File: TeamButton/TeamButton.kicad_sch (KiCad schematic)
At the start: 0 parts

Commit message: Bring in old schematic for cleanup / base work.
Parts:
- added J1: RJ45, symbol Connector:RJ45
- added SW1, SW2: SW_Push, symbol Switch:SW_Push
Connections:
- new net: J1.4, SW2.1
- new net: J1.3, SW2.2
- new net: J1.8, SW1.1
- new net: J1.7, SW1.2
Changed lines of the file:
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@@
 (kicad_sch (version 20221206) (generator eeschema)
   (paper "A4")
-  (symbol_instances)
+  (wire (pts (xy 104.14 72.39) (xy 123.19 72.39))
+    (stroke (width 0) (type default))
+  )
+  (wire (pts (xy 113.03 69.85) (xy 104.14 69.85))
+    (stroke (width 0) (type default))
+  )
+  (wire (pts (xy 123.19 82.55) (xy 104.14 82.55))
+    (stroke (width 0) (type default))
+  )
+  (wire (pts (xy 123.19 72.39) (xy 123.19 69.85))
+    (stroke (width 0) (type default))
+  )
+  (wire (pts (xy 104.14 80.01) (xy 113.03 80.01))
+    (stroke (width 0) (type default))
+  )
+  (wire (pts (xy 123.19 80.01) (xy 123.19 82.55))
+    (stroke (width 0) (type default))
+  )
+  (symbol (lib_id "Switch:SW_Push") (at 118.11 80.01 0) (unit 1)
+    (in_bom yes) (on_board yes) (dnp no) (fields_autoplaced)
+    (property "Reference" "SW2" (at 118.11 73.66 0)
+      (effects (font (size 1.27 1.27)))
+    )
+    (property "Value" "SW_Push" (at 118.11 76.2 0)
+      (effects (font (size 1.27 1.27)))
+    )
+    (property "Footprint" "" (at 118.11 74.93 0)
+      (effects (font (size 1.27 1.27)) hide)
+    )
+    (property "Datasheet" "~" (at 118.11 74.93 0)
+      (effects (font (size 1.27 1.27)) hide)
+    )
+    (pin "1")
+    (pin "2")
+    (instances
+      (project "TeamButton"
+        (path "/a2251e9b-34a9-4b44-9287-d557388f6936"
+          (reference "SW2") (unit 1)
+        )
+      )
+    )
+  )
+  (symbol (lib_id "Switch:SW_Push") (at 118.11 69.85 0) (unit 1)
+    (in_bom yes) (on_board yes) (dnp no) (fields_autoplaced)
+    (property "Reference" "SW1" (at 118.11 63.5 0)
+      (effects (font (size 1.27 1.27)))
+    )
+    (property "Value" "SW_Push" (at 118.11 66.04 0)
+      (effects (font (size 1.27 1.27)))
+    )
+    (property "Footprint" "" (at 118.11 64.77 0)
+      (effects (font (size 1.27 1.27)) hide)
+    )
+    (property "Datasheet" "~" (at 118.11 64.77 0)
+      (effects (font (size 1.27 1.27)) hide)
+    )
+    (pin "1")
+    (pin "2")
+    (instances
+      (project "TeamButton"
+        (path "/a2251e9b-34a9-4b44-9287-d557388f6936"
+          (reference "SW1") (unit 1)
+        )
+      )
+    )
+  )
+  (symbol (lib_id "Connector:RJ45") (at 93.98 80.01 0) (unit 1)
+    (in_bom yes) (on_board yes) (dnp no) (fields_autoplaced)
+    (property "Reference" "J1" (at 93.98 63.5 0)
+      (effects (font (size 1.27 1.27)))
+    )
+    (property "Value" "RJ45" (at 93.98 66.04 0)
+      (effects (font (size 1.27 1.27)))
+    )
+    (property "Footprint" "" (at 93.98 79.375 90)
+      (effects (font (size 1.27 1.27)) hide)
+    )
+    (property "Datasheet" "~" (at 93.98 79.375 90)
+      (effects (font (size 1.27 1.27)) hide)
+    )
+    (pin "1")
+    (pin "2")
+    (pin "3")
+    (pin "4")
+    (pin "5")
+    (pin "6")
+    (pin "7")
+    (pin "8")
+    (instances
+      (project "TeamButton"
+        (path "/a2251e9b-34a9-4b44-9287-d557388f6936"
+          (reference "J1") (unit 1)
+        )
+      )
+    )
+  )
+  (sheet_instances
+    (path "/" (page "1"))
+  )
 )

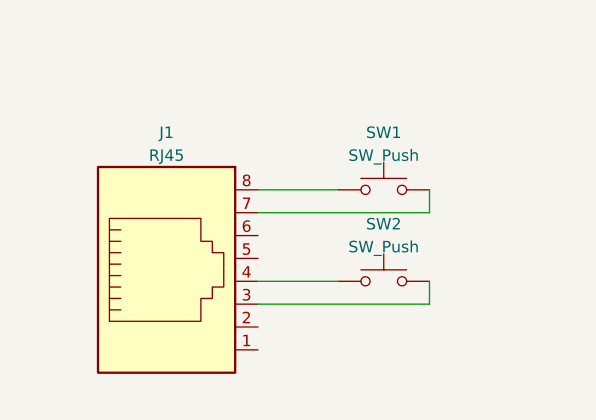
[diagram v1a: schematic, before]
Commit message: Added new files, swap to new FET for toggling, added FET as symbols.
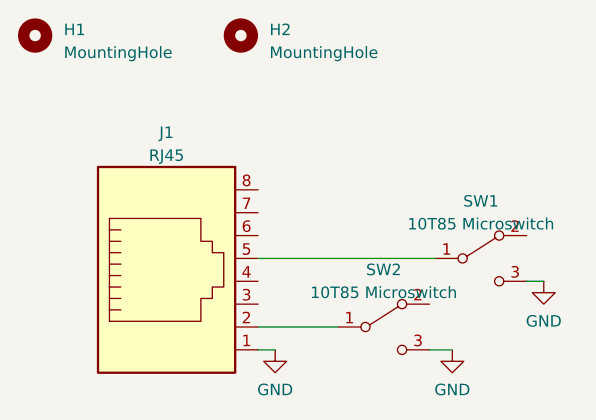
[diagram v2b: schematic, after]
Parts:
- removed SW1, SW2: SW_Push, symbol Switch:SW_Push
- added H1, H2: MountingHole, MountingHole:MountingHole_2.7mm_M2.5_DIN965, symbol Mechanical:MountingHole
- added SW1, SW2: 10T85 Microswitch, footprints:10T85 Microswitch, symbol symbols:10T85 Microswitch
- J1: footprint (none) -> footprints:RCH RC00139
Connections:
- net GND: now reaches J1.1
- net GND: now also SW1.3 (NO), SW2.3 (NO)
- net at J1.2: now also SW2.1 (C)
- net at J1.5: now also SW1.1 (C)
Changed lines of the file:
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@@
-(kicad_sch (version 20221206) (generator eeschema)
+(kicad_sch (version 20230121) (generator eeschema)
   (paper "A4")
-  (wire (pts (xy 104.14 72.39) (xy 123.19 72.39))
+  (wire (pts (xy 104.14 77.47) (xy 123.825 77.47))
     (stroke (width 0) (type default))
   )
-  (wire (pts (xy 113.03 69.85) (xy 104.14 69.85))
+  (wire (pts (xy 104.14 87.63) (xy 106.045 87.63))
     (stroke (width 0) (type default))
   )
-  (wire (pts (xy 123.19 82.55) (xy 104.14 82.55))
+  (wire (pts (xy 104.14 85.09) (xy 113.03 85.09))
     (stroke (width 0) (type default))
   )
-  (wire (pts (xy 123.19 72.39) (xy 123.19 69.85))
+  (wire (pts (xy 135.89 80.01) (xy 133.985 80.01))
     (stroke (width 0) (type default))
   )
-  (wire (pts (xy 104.14 80.01) (xy 113.03 80.01))
+  (wire (pts (xy 125.73 87.63) (xy 123.19 87.63))
     (stroke (width 0) (type default))
   )
-  (wire (pts (xy 123.19 80.01) (xy 123.19 82.55))
-    (stroke (width 0) (type default))
-  )
-  (symbol (lib_id "Switch:SW_Push") (at 118.11 80.01 0) (unit 1)
+  (symbol (lib_id "power:GND") (at 125.73 87.63 0) (unit 1)
     (in_bom yes) (on_board yes) (dnp no) (fields_autoplaced)
-    (property "Reference" "SW2" (at 118.11 73.66 0)
+    (property "Reference" "#PWR04" (at 125.73 93.98 0)
+      (effects (font (size 1.27 1.27)) hide)
+    )
+    (property "Value" "GND" (at 125.73 92.075 0)
       (effects (font (size 1.27 1.27)))
     )
-    (property "Value" "SW_Push" (at 118.11 76.2 0)
+    (property "Footprint" "" (at 125.73 87.63 0)
+      (effects (font (size 1.27 1.27)) hide)
+    )
+    (property "Datasheet" "" (at 125.73 87.63 0)
+      (effects (font (size 1.27 1.27)) hide)
+    )
+    (pin "1")
+    (instances
+      (project "TeamButton"
+        (path "/a2251e9b-34a9-4b44-9287-d557388f6936"
+          (reference "#PWR04") (unit 1)
+        )
+      )
+    )
+  )
+  (symbol (lib_id "power:GND") (at 106.045 87.63 0) (unit 1)
+    (in_bom yes) (on_board yes) (dnp no) (fields_autoplaced)
+    (property "Reference" "#PWR03" (at 106.045 93.98 0)
+      (effects (font (size 1.27 1.27)) hide)
+    )
+    (property "Value" "GND" (at 106.045 92.075 0)
       (effects (font (size 1.27 1.27)))
     )
-    (property "Footprint" "" (at 118.11 74.93 0)
+    (property "Footprint" "" (at 106.045 87.63 0)
       (effects (font (size 1.27 1.27)) hide)
     )
-    (property "Datasheet" "~" (at 118.11 74.93 0)
+    (property "Datasheet" "" (at 106.045 87.63 0)
+      (effects (font (size 1.27 1.27)) hide)
+    )
+    (pin "1")
+    (instances
+      (project "TeamButton"
+        (path "/a2251e9b-34a9-4b44-9287-d557388f6936"
+          (reference "#PWR03") (unit 1)
+        )
+      )
+    )
+  )
+  (symbol (lib_id "Mechanical:MountingHole") (at 79.375 52.705 0) (unit 1)
+    (in_bom yes) (on_board yes) (dnp no) (fields_autoplaced)
+    (property "Reference" "H1" (at 82.55 52.07 0)
+      (effects (font (size 1.27 1.27)) (justify left))
+    )
+    (property "Value" "MountingHole" (at 82.55 54.61 0)
+      (effects (font (size 1.27 1.27)) (justify left))
+    )
+    (property "Footprint" "MountingHole:MountingHole_2.7mm_M2.5_DIN965" (at 79.375 52.705 0)
+      (effects (font (size 1.27 1.27)) hide)
+    )
+    (property "Datasheet" "~" (at 79.375 52.705 0)
+      (effects (font (size 1.27 1.27)) hide)
+    )
+    (instances
+      (project "TeamButton"
+        (path "/a2251e9b-34a9-4b44-9287-d557388f6936"
+          (reference "H1") (unit 1)
+        )
+      )
+    )
+  )
+  (symbol (lib_id "symbols:10T85 Microswitch") (at 118.11 85.09 0) (unit 1)
+    (in_bom yes) (on_board yes) (dnp no) (fields_autoplaced)
+    (property "Reference" "SW2" (at 118.11 78.74 0)
+      (effects (font (size 1.27 1.27)))
+    )
+    (property "Value" "10T85 Microswitch" (at 118.11 81.28 0)
+      (effects (font (size 1.27 1.27)))
+    )
+    (property "Footprint" "footprints:10T85 Microswitch" (at 118.11 92.71 0)
+      (effects (font (size 1.27 1.27)) hide)
+    )
+    (property "Datasheet" "~" (at 118.11 85.09 0)
       (effects (font (size 1.27 1.27)) hide)
     )
     (pin "1")
     (pin "2")
+    (pin "3")
     (instances
       (project "TeamButton"
@@
     )
   )
-  (symbol (lib_id "Switch:SW_Push") (at 118.11 69.85 0) (unit 1)
+  (symbol (lib_id "power:GND") (at 135.89 80.01 0) (unit 1)
     (in_bom yes) (on_board yes) (dnp no) (fields_autoplaced)
-    (property "Reference" "SW1" (at 118.11 63.5 0)
+    (property "Reference" "#PWR05" (at 135.89 86.36 0)
+      (effects (font (size 1.27 1.27)) hide)
+    )
+    (property "Value" "GND" (at 135.89 84.455 0)
       (effects (font (size 1.27 1.27)))
     )
-    (property "Value" "SW_Push" (at 118.11 66.04 0)
+    (property "Footprint" "" (at 135.89 80.01 0)
+      (effects (font (size 1.27 1.27)) hide)
+    )
+    (property "Datasheet" "" (at 135.89 80.01 0)
+      (effects (font (size 1.27 1.27)) hide)
+    )
+    (pin "1")
+    (instances
+      (project "TeamButton"
+        (path "/a2251e9b-34a9-4b44-9287-d557388f6936"
+          (reference "#PWR05") (unit 1)
+        )
+      )
+    )
+  )
+  (symbol (lib_id "Mechanical:MountingHole") (at 102.235 52.705 0) (unit 1)
+    (in_bom yes) (on_board yes) (dnp no) (fields_autoplaced)
+    (property "Reference" "H2" (at 105.41 52.07 0)
+      (effects (font (size 1.27 1.27)) (justify left))
+    )
+    (property "Value" "MountingHole" (at 105.41 54.61 0)
+      (effects (font (size 1.27 1.27)) (justify left))
+    )
+    (property "Footprint" "MountingHole:MountingHole_2.7mm_M2.5_DIN965" (at 102.235 52.705 0)
+      (effects (font (size 1.27 1.27)) hide)
+    )
+    (property "Datasheet" "~" (at 102.235 52.705 0)
+      (effects (font (size 1.27 1.27)) hide)
+    )
+    (instances
+      (project "TeamButton"
+        (path "/a2251e9b-34a9-4b44-9287-d557388f6936"
+          (reference "H2") (unit 1)
+        )
+      )
+    )
+  )
+  (symbol (lib_id "symbols:10T85 Microswitch") (at 128.905 77.47 0) (unit 1)
+    (in_bom yes) (on_board yes) (dnp no) (fields_autoplaced)
+    (property "Reference" "SW1" (at 128.905 71.12 0)
       (effects (font (size 1.27 1.27)))
     )
-    (property "Footprint" "" (at 118.11 64.77 0)
+    (property "Value" "10T85 Microswitch" (at 128.905 73.66 0)
+      (effects (font (size 1.27 1.27)))
+    )
+    (property "Footprint" "footprints:10T85 Microswitch" (at 128.905 85.09 0)
       (effects (font (size 1.27 1.27)) hide)
     )
-    (property "Datasheet" "~" (at 118.11 64.77 0)
+    (property "Datasheet" "~" (at 128.905 77.47 0)
       (effects (font (size 1.27 1.27)) hide)
     )
     (pin "1")
     (pin "2")
+    (pin "3")
     (instances
       (project "TeamButton"
@@
       (effects (font (size 1.27 1.27)))
     )
-    (property "Footprint" "" (at 93.98 79.375 90)
+    (property "Footprint" "footprints:RCH RC00139" (at 93.98 79.375 90)
       (effects (font (size 1.27 1.27)) hide)
     )

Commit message: Updated team buttonboard to use M3 fasteners!
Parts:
- H1, H2: footprint MountingHole:MountingHole_2.7mm_M2.5_DIN965 -> MountingHole:MountingHole_3.2mm_M3
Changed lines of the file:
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@@
       (effects (font (size 1.27 1.27)) (justify left))
     )
-    (property "Footprint" "MountingHole:MountingHole_2.7mm_M2.5_DIN965" (at 79.375 52.705 0)
+    (property "Footprint" "MountingHole:MountingHole_3.2mm_M3" (at 79.375 52.705 0)
       (effects (font (size 1.27 1.27)) hide)
     )
@@
       (effects (font (size 1.27 1.27)) (justify left))
     )
-    (property "Footprint" "MountingHole:MountingHole_2.7mm_M2.5_DIN965" (at 102.235 52.705 0)
+    (property "Footprint" "MountingHole:MountingHole_3.2mm_M3" (at 102.235 52.705 0)
       (effects (font (size 1.27 1.27)) hide)
     )

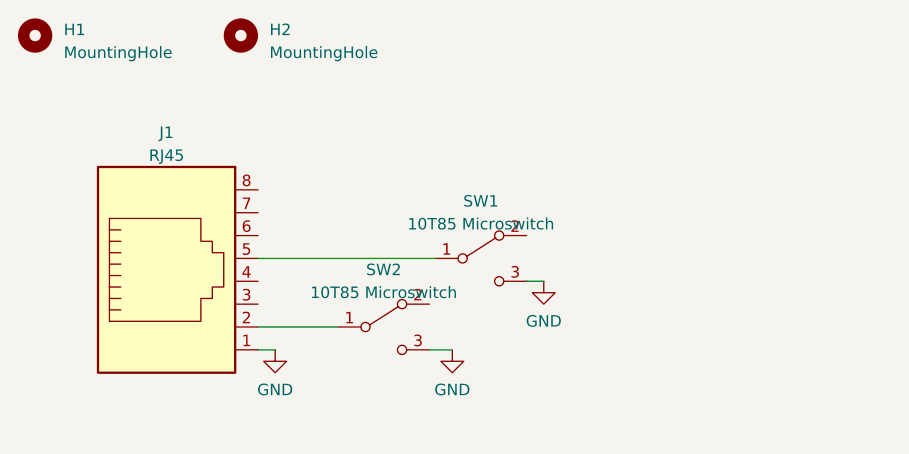
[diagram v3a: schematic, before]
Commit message: Updated Button and Stacklight PCB to not have backwards fucking footprint shit.
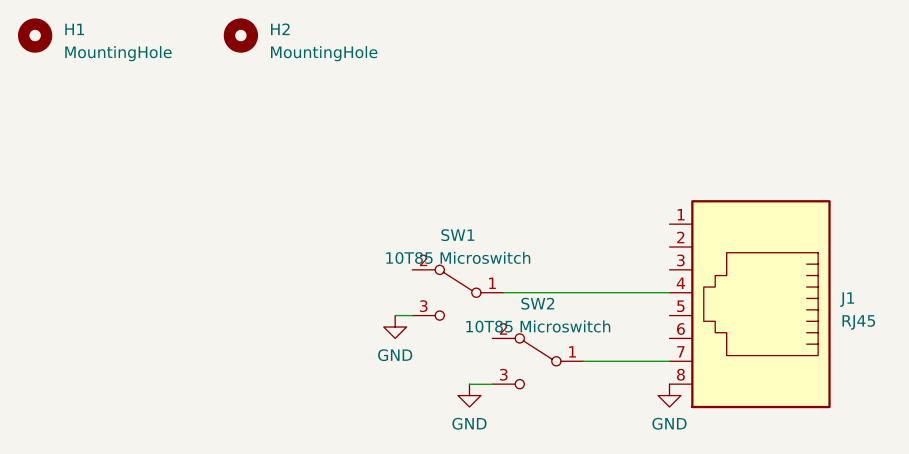
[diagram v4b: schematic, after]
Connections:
- net GND: now also J1.8; no longer J1.1
- net at SW2.1 (C): now also J1.7; no longer J1.2
- net at SW1.1 (C): now also J1.4; no longer J1.5
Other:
- moved on the sheet: J1, SW1, SW2
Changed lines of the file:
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@@
 (kicad_sch (version 20230121) (generator eeschema)
   (paper "A4")
-  (wire (pts (xy 104.14 77.47) (xy 123.825 77.47))
+  (wire (pts (xy 140.335 88.9) (xy 149.86 88.9))
     (stroke (width 0) (type default))
   )
-  (wire (pts (xy 104.14 87.63) (xy 106.045 87.63))
+  (wire (pts (xy 119.38 83.82) (xy 121.285 83.82))
     (stroke (width 0) (type default))
   )
-  (wire (pts (xy 104.14 85.09) (xy 113.03 85.09))
+  (wire (pts (xy 127.635 91.44) (xy 130.175 91.44))
     (stroke (width 0) (type default))
   )
-  (wire (pts (xy 135.89 80.01) (xy 133.985 80.01))
+  (wire (pts (xy 131.445 81.28) (xy 149.86 81.28))
     (stroke (width 0) (type default))
   )
-  (wire (pts (xy 125.73 87.63) (xy 123.19 87.63))
-    (stroke (width 0) (type default))
-  )
-  (symbol (lib_id "power:GND") (at 125.73 87.63 0) (unit 1)
+  (symbol (lib_id "power:GND") (at 127.635 91.44 0) (mirror y) (unit 1)
     (in_bom yes) (on_board yes) (dnp no) (fields_autoplaced)
-    (property "Reference" "#PWR04" (at 125.73 93.98 0)
+    (property "Reference" "#PWR04" (at 127.635 97.79 0)
       (effects (font (size 1.27 1.27)) hide)
     )
-    (property "Value" "GND" (at 125.73 92.075 0)
+    (property "Value" "GND" (at 127.635 95.885 0)
       (effects (font (size 1.27 1.27)))
     )
-    (property "Footprint" "" (at 125.73 87.63 0)
+    (property "Footprint" "" (at 127.635 91.44 0)
       (effects (font (size 1.27 1.27)) hide)
     )
-    (property "Datasheet" "" (at 125.73 87.63 0)
+    (property "Datasheet" "" (at 127.635 91.44 0)
       (effects (font (size 1.27 1.27)) hide)
     )
@@
     )
   )
-  (symbol (lib_id "power:GND") (at 106.045 87.63 0) (unit 1)
+  (symbol (lib_id "power:GND") (at 149.86 91.44 0) (unit 1)
     (in_bom yes) (on_board yes) (dnp no) (fields_autoplaced)
-    (property "Reference" "#PWR03" (at 106.045 93.98 0)
+    (property "Reference" "#PWR03" (at 149.86 97.79 0)
       (effects (font (size 1.27 1.27)) hide)
     )
-    (property "Value" "GND" (at 106.045 92.075 0)
+    (property "Value" "GND" (at 149.86 95.885 0)
       (effects (font (size 1.27 1.27)))
     )
-    (property "Footprint" "" (at 106.045 87.63 0)
+    (property "Footprint" "" (at 149.86 91.44 0)
       (effects (font (size 1.27 1.27)) hide)
     )
-    (property "Datasheet" "" (at 106.045 87.63 0)
+    (property "Datasheet" "" (at 149.86 91.44 0)
       (effects (font (size 1.27 1.27)) hide)
     )
@@
     )
   )
-  (symbol (lib_id "symbols:10T85 Microswitch") (at 118.11 85.09 0) (unit 1)
+  (symbol (lib_id "symbols:10T85 Microswitch") (at 135.255 88.9 0) (mirror y) (unit 1)
     (in_bom yes) (on_board yes) (dnp no) (fields_autoplaced)
-    (property "Reference" "SW2" (at 118.11 78.74 0)
+    (property "Reference" "SW2" (at 135.255 82.55 0)
       (effects (font (size 1.27 1.27)))
     )
-    (property "Value" "10T85 Microswitch" (at 118.11 81.28 0)
+    (property "Value" "10T85 Microswitch" (at 135.255 85.09 0)
       (effects (font (size 1.27 1.27)))
     )
-    (property "Footprint" "footprints:10T85 Microswitch" (at 118.11 92.71 0)
+    (property "Footprint" "footprints:10T85 Microswitch" (at 135.255 96.52 0)
       (effects (font (size 1.27 1.27)) hide)
     )
-    (property "Datasheet" "~" (at 118.11 85.09 0)
+    (property "Datasheet" "~" (at 135.255 88.9 0)
       (effects (font (size 1.27 1.27)) hide)
     )
@@
     )
   )
-  (symbol (lib_id "power:GND") (at 135.89 80.01 0) (unit 1)
+  (symbol (lib_id "power:GND") (at 119.38 83.82 0) (mirror y) (unit 1)
     (in_bom yes) (on_board yes) (dnp no) (fields_autoplaced)
-    (property "Reference" "#PWR05" (at 135.89 86.36 0)
+    (property "Reference" "#PWR05" (at 119.38 90.17 0)
       (effects (font (size 1.27 1.27)) hide)
     )
-    (property "Value" "GND" (at 135.89 84.455 0)
+    (property "Value" "GND" (at 119.38 88.265 0)
       (effects (font (size 1.27 1.27)))
     )
-    (property "Footprint" "" (at 135.89 80.01 0)
+    (property "Footprint" "" (at 119.38 83.82 0)
       (effects (font (size 1.27 1.27)) hide)
     )
-    (property "Datasheet" "" (at 135.89 80.01 0)
+    (property "Datasheet" "" (at 119.38 83.82 0)
       (effects (font (size 1.27 1.27)) hide)
     )
@@
     )
   )
-  (symbol (lib_id "symbols:10T85 Microswitch") (at 128.905 77.47 0) (unit 1)
+  (symbol (lib_id "symbols:10T85 Microswitch") (at 126.365 81.28 0) (mirror y) (unit 1)
     (in_bom yes) (on_board yes) (dnp no) (fields_autoplaced)
-    (property "Reference" "SW1" (at 128.905 71.12 0)
+    (property "Reference" "SW1" (at 126.365 74.93 0)
       (effects (font (size 1.27 1.27)))
     )
-    (property "Value" "10T85 Microswitch" (at 128.905 73.66 0)
+    (property "Value" "10T85 Microswitch" (at 126.365 77.47 0)
       (effects (font (size 1.27 1.27)))
     )
-    (property "Footprint" "footprints:10T85 Microswitch" (at 128.905 85.09 0)
+    (property "Footprint" "footprints:10T85 Microswitch" (at 126.365 88.9 0)
       (effects (font (size 1.27 1.27)) hide)
     )
-    (property "Datasheet" "~" (at 128.905 77.47 0)
+    (property "Datasheet" "~" (at 126.365 81.28 0)
       (effects (font (size 1.27 1.27)) hide)
     )
@@
     )
   )
-  (symbol (lib_id "Connector:RJ45") (at 93.98 80.01 0) (unit 1)
+  (symbol (lib_id "Connector:RJ45") (at 160.02 81.28 180) (unit 1)
     (in_bom yes) (on_board yes) (dnp no) (fields_autoplaced)
-    (property "Reference" "J1" (at 93.98 63.5 0)
-      (effects (font (size 1.27 1.27)))
+    (property "Reference" "J1" (at 168.91 81.915 0)
+      (effects (font (size 1.27 1.27)) (justify right))
     )
-    (property "Value" "RJ45" (at 93.98 66.04 0)
-      (effects (font (size 1.27 1.27)))
+    (property "Value" "RJ45" (at 168.91 84.455 0)
+      (effects (font (size 1.27 1.27)) (justify right))
     )
-    (property "Footprint" "footprints:RCH RC00139" (at 93.98 79.375 90)
+    (property "Footprint" "footprints:RCH RC00139" (at 160.02 81.915 90)
       (effects (font (size 1.27 1.27)) hide)
     )
-    (property "Datasheet" "~" (at 93.98 79.375 90)
+    (property "Datasheet" "~" (at 160.02 81.915 90)
       (effects (font (size 1.27 1.27)) hide)
     )

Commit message: Added spacer mounting holes to board in case are needed.  Insert through back first.  Use smaller fasteners, etc.  Only one hole should be needed.
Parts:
- SW1, SW2: footprint footprints:10T85 Microswitch -> footprints:10T85 Microswitch with M3 mounts
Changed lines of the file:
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@@
       (effects (font (size 1.27 1.27)))
     )
-    (property "Footprint" "footprints:10T85 Microswitch" (at 135.255 96.52 0)
+    (property "Footprint" "footprints:10T85 Microswitch with M3 mounts" (at 135.255 96.52 0)
       (effects (font (size 1.27 1.27)) hide)
     )
@@
       (effects (font (size 1.27 1.27)))
     )
-    (property "Footprint" "footprints:10T85 Microswitch" (at 126.365 88.9 0)
+    (property "Footprint" "footprints:10T85 Microswitch with M3 mounts" (at 126.365 88.9 0)
       (effects (font (size 1.27 1.27)) hide)
     )
